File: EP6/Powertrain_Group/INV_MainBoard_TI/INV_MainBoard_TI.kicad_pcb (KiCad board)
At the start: 4 copper layers, 100 x 92 mm, 259 parts, among them IC1 LM26420Q0XMHX_NOPB, J1 FX26-30P-1SV, J10 CAN, J11 CAN, J12 CAN, J13 motorTemp, J14 LVBattery, J15 PWMDAC, J2 motorSense, J3 LVBattery, J4 JTAG, J5 current_DC, J6 to PhaseIsense, J7 phase control monitor, J8 current, J9 CAN, Q1 2N7002, Q2 2N7002, SW1 TS-1187A-B-A-B, U1 LM324D, U10 LM2903, U11 LM2903, U12 LM2903, U13 LM2903, U14 OPA340NA, U15 LM2903, U2 TPS5430DDAR, U21 OPA340NA, U22 tms320f28377s, U23 REF3133AQDBZRQ1, U24 REF3133AQDBZRQ1, U3 OPA340NA, U4 TCAN1042VDRQ1, U5 CAT24C256, U6 TCAN1042VDRQ1, U7 OPA340NA, U8 OPA340NA, U9 OPA340NA, Y1 ABM3BAIG-10.000MHZ-12-1Z-T

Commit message: update INV_MainBoard_TI to V1.1
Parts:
- removed JP2: TRST, Jumper:SolderJumper-2_P1.3mm_Bridged_Pad1.0x1.5mm
- removed U21: OPA340NA, Package_TO_SOT_SMD:SOT-23-5
- added C100: 680p, Capacitor_SMD:C_0402_1005Metric, F.Cu at (165.4, 125.6)
- added C101: 680p, Capacitor_SMD:C_0402_1005Metric, F.Cu at (154.1, 127.4)
- added C102: 680p, Capacitor_SMD:C_0402_1005Metric, F.Cu at (143.0, 129.7)
- added C103: 100n, Capacitor_SMD:C_0402_1005Metric, F.Cu at (179.7, 131.7)
- added C104: 100n, Capacitor_SMD:C_0402_1005Metric, F.Cu at (178.7, 127.3)
- added C105: 100n, Capacitor_SMD:C_0402_1005Metric, F.Cu at (118.6, 140.8)
- added C106: 100n, Capacitor_SMD:C_0402_1005Metric, F.Cu at (172.3, 114.5)
- added C107: 100n, Capacitor_SMD:C_0402_1005Metric, F.Cu at (167.7, 119.7)
- added C108: 100n, Capacitor_SMD:C_0402_1005Metric, F.Cu at (156.4, 121.5)
- added C109: 100n, Capacitor_SMD:C_0402_1005Metric, F.Cu at (145.3, 123.8)
- added C110: 100n, Capacitor_SMD:C_0402_1005Metric, F.Cu at (124.7, 115.6)
- added C111: 100n, Capacitor_SMD:C_0402_1005Metric, F.Cu at (128.1, 119.5)
- added C112: 22p, Capacitor_SMD:C_0402_1005Metric, F.Cu at (131.7, 58.1)
- added C113: 22p, Capacitor_SMD:C_0402_1005Metric, F.Cu at (131.7, 61.9)
- added C114: 22p, Capacitor_SMD:C_0402_1005Metric, F.Cu at (131.7, 68.8)
- added C115: 22p, Capacitor_SMD:C_0402_1005Metric, F.Cu at (131.7, 72.7)
- added C116: 4u7 10v, Capacitor_SMD:C_0402_1005Metric, F.Cu at (145.0, 61.6)
- added C117: 4u7 10v, Capacitor_SMD:C_0402_1005Metric, F.Cu at (145.0, 68.1)
- added C59: 43p, Capacitor_SMD:C_0402_1005Metric, F.Cu at (118.4, 113.3)
- added C85: 43p, Capacitor_SMD:C_0402_1005Metric, F.Cu at (120.0, 118.0)
- added C86: 100n, Capacitor_SMD:C_0402_1005Metric, F.Cu at (121.2, 115.6)
- added C95: 100n, Capacitor_SMD:C_0402_1005Metric, F.Cu at (127.5, 116.7)
- added C96: 1u, Capacitor_SMD:C_0402_1005Metric, F.Cu at (124.6, 143.1)
- added C99: 680p, Capacitor_SMD:C_0402_1005Metric, F.Cu at (178.2, 116.8)
- added D10: YELLOW LED, LED_SMD:LED_0603_1608Metric, F.Cu at (164.0, 106.8)
- added D11: LED50, LED_SMD:LED_0603_1608Metric, F.Cu at (165.6, 106.8)
- added D12: LED50, LED_SMD:LED_0603_1608Metric, F.Cu at (167.2, 106.8)
- added D13: LED50, LED_SMD:LED_0603_1608Metric, F.Cu at (168.8, 106.8)
- added D14: LED50, LED_SMD:LED_0603_1608Metric, F.Cu at (170.4, 106.8)
- added FB15: GZ1608D601TF, Capacitor_SMD:C_0603_1608Metric, F.Cu at (144.7, 121.3)
- added R78: 2k2, Resistor_SMD:R_0402_1005Metric, F.Cu at (165.7, 104.3)
- added SW2: BUT39, Button_Switch_SMD:SW_Tactile_SPST_NO_Straight_CK_PTS636Sx25SMTRLFS, F.Cu at (165.0, 113.7)
- added SW3: BUT58, Button_Switch_SMD:SW_Tactile_SPST_NO_Straight_CK_PTS636Sx25SMTRLFS, F.Cu at (169.6, 96.4)
- added U16: INA333AIDGK, PCM_Package_SO_AKL:MSOP-8_3x3mm_P0.65mm, F.Cu at (122.1, 113.3)
- added U17: INA333AIDGK, PCM_Package_SO_AKL:MSOP-8_3x3mm_P0.65mm, F.Cu at (123.8, 117.9)
- added U18: OPA340NA, Package_TO_SOT_SMD:SOT-23-5, F.Cu at (179.4, 129.5)
- C20, C21, C40, C41, C42, C43, C46, C47, C48, C49, C53, C54: value 0u1 -> 100n
- R17, R72: value 120R -> 90R
- R19, R20, R21, R22: value 10k -> 10k 0.1%
- R23, R24, R25, R26, R63, R64, R65: value 20k -> 10k
- R29, R55: value 22k -> 2k4
- R3: value 20k -> 1k
- R30, R54: value 82k -> 10k
- R31, R50, R52, R57, R59, R61: value 22k -> 10k
- R33, R51, R53, R56, R58, R60: value 82k -> 28k
- R34, R38: value 20k -> 10k 0.1%
- R35, R36, R37, R39, R40, R41, R43, R44, R45, R47, R48, R49: value 20k -> 100R
- R42, R46, R62: value 20k -> 2k2
- R68: value 10k -> 2k2
- SW1: footprint Button_Switch_SMD:SW_Push_1P1T_XKB_TS-1187A -> Button_Switch_SMD:SW_SPST_TL3342
- U1: value LM324D -> OPA340NA; footprint PCM_Package_SO_AKL:SOIC-14_3.9x8.7mm_P1.27mm -> Package_TO_SOT_SMD:SOT-23-5
- U14, U3, U7, U8, U9: value OPA340NA -> INA333AIDGK; footprint Package_TO_SOT_SMD:SOT-23-5 -> PCM_Package_SO_AKL:MSOP-8_3x3mm_P0.65mm
- moved U3 62.9 mm to (120.9, 143.1), turned to 180 degrees
- moved R34 60.5 mm to (119.1, 118.0), turned to 90 degrees
- moved R69 53.4 mm to (171.4, 78.5)
- moved R38 51.9 mm to (117.4, 113.3)
- moved C54 49.1 mm to (131.2, 125.8), turned to 180 degrees
- moved C53 48.9 mm to (131.1, 120.4)
- moved R26 48.4 mm to (178.7, 126.3), turned to 0 degrees
- moved R25 47.9 mm to (176.8, 129.5), turned to 90 degrees
- moved FB3 42.6 mm to (132.8, 119.4), turned to -90 degrees
- moved R62 42.6 mm to (168.7, 104.3), turned to -90 degrees
- moved FB5 38.5 mm to (119.9, 138.5)
- moved R46 38.0 mm to (167.7, 104.3), turned to -90 degrees
- moved FB6 36.9 mm to (178.4, 114.0)
- moved R42 30.3 mm to (166.7, 104.3), turned to -90 degrees
- moved R68 27.4 mm to (169.7, 104.3)
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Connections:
- net /Isense&motT_OCP&OTP/IsenseNode1/IN+ renamed /Isense&motT_OCP&OTP/U+
- net /Isense&motT_OCP&OTP/IsenseNode1/IN- renamed /Isense&motT_OCP&OTP/U-
- net /Isense&motT_OCP&OTP/IsenseNode2/IN+ renamed /Isense&motT_OCP&OTP/V+
- net /Isense&motT_OCP&OTP/IsenseNode2/IN- renamed /Isense&motT_OCP&OTP/V-
- net /Isense&motT_OCP&OTP/IsenseNode3/IN+ renamed /Isense&motT_OCP&OTP/W+
- net /Isense&motT_OCP&OTP/IsenseNode3/IN- renamed /Isense&motT_OCP&OTP/W-
- net /Isense&motT_OCP&OTP/OCPnode/filt5V renamed /Isense&motT_OCP&OTP/OCPnode/filt3V3
- net /Isense&motT_OCP&OTP/OCPnode1/filt5V renamed /Isense&motT_OCP&OTP/OCPnode1/filt3V3
- net /Isense&motT_OCP&OTP/OCPnode2/filt5V renamed /Isense&motT_OCP&OTP/OCPnode2/filt3V3
- net /Isense&motT_OCP&OTP/OCPnode3/filt5V renamed /Isense&motT_OCP&OTP/OCPnode3/filt3V3
- net /Isense&motT_OCP&OTP/filt5V renamed /Isense&motT_OCP&OTP/filt3V3
- net /MCU/TCK renamed /MCU/RTCK
- net Net-(J4-Pin_13) renamed /MCU/EMU0
- net Net-(J4-Pin_14) renamed /MCU/EMU1
- net Net-(J4-Pin_5) renamed /MCU/PD
- C21 pad 1: Net-(U3-V+) -> +5V
- C40 pad 1: Net-(U7-V+) -> +5V
- C41 pad 1: Net-(U8-V+) -> +5V
- C42 pad 1: Net-(U9-V+) -> +5V
- C43 pad 1: Net-(U14-V+) -> +5V
- C53 pad 1: Net-(U21-V+) -> Net-(U1-V+)
- C54 pad 1: Net-(U21--) -> Net-(U1--)
- FB1 pad 1: +5V -> +3V3
- FB10 pad 1: +3V3 -> Net-(U8-REF)
- FB10 pad 2: Net-(U21-V+) -> /Isense&motT_OCP&OTP/Vref_1.65V
- FB11 pad 1: +5V -> +3V3
- FB13 pad 1: +5V -> Net-(U9-REF)
- FB13 pad 2: Net-(U14-V+) -> /Isense&motT_OCP&OTP/Vref_1.65V
- FB3 pad 1: +5V -> +3V3
- FB3 pad 2: Net-(U3-V+) -> Net-(U1-V+)
- FB4 pad 1: +5V -> +3V3
- FB4 pad 2: Net-(U7-V+) -> Net-(U18-V+)
- FB5 pad 1: +5V -> Net-(U3-REF)
- FB5 pad 2: Net-(U8-V+) -> /Isense&motT_OCP&OTP/Vref_1.65V
- FB6 pad 1: +5V -> Net-(U7-REF)
- FB6 pad 2: Net-(U9-V+) -> /Isense&motT_OCP&OTP/Vref_1.65V
- FB7 pad 1: +5V -> +3V3
- FB8 pad 1: +5V -> +3V3
- FB9 pad 1: +5V -> +3V3
- J4 pad 2: Net-(J4-Pin_2) -> /MCU/TRST
- R19 pad 1: Net-(U1B--) -> /SIN+
- R19 pad 2: /EncoderDifVconverter/sin-3V3_out -> Net-(U16--)
- R20 pad 1: Net-(U1A--) -> /SIN-
- R20 pad 2: /EncoderDifVconverter/sin+3V3_out -> Net-(U16-+)
- R21 pad 1: Net-(U1D--) -> /COS+
- R21 pad 2: /EncoderDifVconverter/cos+3V3_out -> Net-(U17--)
- R22 pad 1: Net-(U1C--) -> /COS-
- R22 pad 2: /EncoderDifVconverter/cos-3V3_out -> Net-(U17-+)
- R23 pad 1: /EncoderDifVconverter/sin-3V3_out -> Net-(U1-V+)
- R23 pad 2: GND -> Net-(U1--)
- R24 pad 1: /EncoderDifVconverter/sin+3V3_out -> Net-(U1--)
- R25 pad 1: /EncoderDifVconverter/cos+3V3_out -> Net-(U18-V+)
- R25 pad 2: GND -> Net-(U18--)
- R26 pad 1: /EncoderDifVconverter/cos-3V3_out -> Net-(U18--)
- R34 pad 1: Net-(U3-+) -> Net-(U17-+)
- R34 pad 2: /Isense&motT_OCP&OTP/Vref_1.65V -> Net-(U17--)
- R35 pad 2: Net-(U3-+) -> Net-(U7--)
- R36 pad 2: Net-(U3--) -> Net-(U7-+)
- R37 pad 1: Net-(U3--) -> Net-(R37-Pad1)
- R37 pad 2: /Isense&motT_OCP&OTP/Isense_DC -> Net-(R37-Pad2)
- R38 pad 1: Net-(U7-+) -> Net-(U16-+)
- R38 pad 2: /Isense&motT_OCP&OTP/Vref_1.65V -> Net-(U16--)
- R39 pad 2: Net-(U7-+) -> Net-(U8--)
- R40 pad 2: Net-(U7--) -> Net-(U8-+)
- R41 pad 1: Net-(U7--) -> Net-(R41-Pad1)
- R41 pad 2: /Isense&motT_OCP&OTP/Isense_U -> Net-(R41-Pad2)
- R42 pad 1: Net-(U8-+) -> /MCU/LED50
- R42 pad 2: /Isense&motT_OCP&OTP/Vref_1.65V -> Net-(D11-A)
- R43 pad 2: Net-(U8-+) -> Net-(U9--)
- R44 pad 2: Net-(U8--) -> Net-(U9-+)
- R45 pad 1: Net-(U8--) -> Net-(R45-Pad1)
- R45 pad 2: /Isense&motT_OCP&OTP/Isense_V -> Net-(R45-Pad2)
- R46 pad 1: Net-(U9-+) -> /MCU/LED51
- R46 pad 2: /Isense&motT_OCP&OTP/Vref_1.65V -> Net-(D12-A)
- R47 pad 2: Net-(U9-+) -> Net-(U14--)
- R48 pad 2: Net-(U9--) -> Net-(U14-+)
- R49 pad 1: Net-(U9--) -> Net-(R49-Pad1)
- R49 pad 2: /Isense&motT_OCP&OTP/Isense_W -> Net-(R49-Pad2)
- R62 pad 1: Net-(U14-+) -> /MCU/LED52
- R62 pad 2: /Isense&motT_OCP&OTP/Vref_1.65V -> Net-(D13-A)
- R63 pad 2: Net-(U14-+) -> Net-(U3--)
- R64 pad 2: Net-(U14--) -> Net-(U3-+)
- R65 pad 1: Net-(U14--) -> Net-(R65-Pad1)
- R65 pad 2: /T_mot -> Net-(R65-Pad2)
- R68 pad 1: Net-(U21-V+) -> /MCU/LED53
- R68 pad 2: Net-(U21--) -> Net-(D14-A)
- R69 pad 1: Net-(U21--) -> +3V3
- R69 pad 2: GND -> /MCU/RST
- TP5 pad 1: /EncoderDifVconverter/sin-3V3_out -> /EncoderDifVconverter/sin+3V3_out
- TP6 pad 1: /EncoderDifVconverter/sin+3V3_out -> /EncoderDifVconverter/Vref_1.65V
- TP8 pad 1: /EncoderDifVconverter/cos-3V3_out -> /EncoderDifVconverter/Vref_1.65V
- U1 pad 1: Net-(U1A--) -> /EncoderDifVconverter/Vref_1.65V
- U1 pad 2: Net-(U1A--) -> GND
- U1 pad 3: /SIN- -> /EncoderDifVconverter/Vref_1.65V
- U1 pad 4: +5V -> Net-(U1--)
- U1 pad 5: /SIN+ -> Net-(U1-V+)
- U14 pad 1: /T_mot -> Net-(R49-Pad2)
- U14 pad 2: GND -> Net-(U14--)
- U14 pad 4: Net-(U14--) -> GND
- U14 pad 5: Net-(U14-V+) -> Net-(U14-REF)
- U22 pad 103: unconnected-(U22D-GPIO58-Pad103) -> /MCU/Button58
- U22 pad 47: /EncoderDifVconverter/sin-3V3_out -> /EncoderDifVconverter/Vref_1.65V
- U22 pad 49: /EncoderDifVconverter/cos-3V3_out -> /EncoderDifVconverter/Vref_1.65V
- U22 pad 86: unconnected-(U22C-GPIO39-Pad86) -> /MCU/Button39
- U22 pad 92: unconnected-(U22B-ERRORSTS-Pad92) -> Net-(U22B-ERRORSTS)
- U22 pad 94: unconnected-(U22D-GPIO50-Pad94) -> /MCU/LED50
- U22 pad 95: unconnected-(U22D-GPIO51-Pad95) -> /MCU/LED51
- U22 pad 96: unconnected-(U22D-GPIO52-Pad96) -> /MCU/LED52
- U22 pad 97: unconnected-(U22D-GPIO53-Pad97) -> /MCU/LED53
- U3 pad 1: /Isense&motT_OCP&OTP/Isense_DC -> Net-(R65-Pad2)
- U3 pad 2: GND -> Net-(U3--)
- U3 pad 4: Net-(U3--) -> GND
- U3 pad 5: Net-(U3-V+) -> Net-(U3-REF)
- U7 pad 1: /Isense&motT_OCP&OTP/Isense_U -> Net-(R37-Pad2)
- U7 pad 2: GND -> Net-(U7--)
- U7 pad 4: Net-(U7--) -> GND
- U7 pad 5: Net-(U7-V+) -> Net-(U7-REF)
- U8 pad 1: /Isense&motT_OCP&OTP/Isense_V -> Net-(R41-Pad2)
- U8 pad 2: GND -> Net-(U8--)
- U8 pad 4: Net-(U8--) -> GND
- U8 pad 5: Net-(U8-V+) -> Net-(U8-REF)
- U9 pad 1: /Isense&motT_OCP&OTP/Isense_W -> Net-(R45-Pad2)
- U9 pad 2: GND -> Net-(U9--)
- U9 pad 4: Net-(U9--) -> GND
- U9 pad 5: Net-(U9-V+) -> Net-(U9-REF)
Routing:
- net +3V3: track 220.0 -> 317.6 mm, vias 4 -> 12
- net /EncoderDifVconverter/Vref_1.65V: track 0.00 -> 56.1 mm
- net /Isense&motT_OCP&OTP/Vref_1.65V: track 60.8 -> 99.0 mm, vias 7 -> 6
- net /T_mot: track 98.0 -> 63.7 mm
- net GND: track 245.7 -> 273.2 mm, vias 168 -> 180
- net /MCU/TRST: track 30.1 -> 52.2 mm
- net +5V: track 76.6 -> 98.1 mm, vias 17 -> 13
- net Net-(J4-Pin_2): track 19.1 -> 0.00 mm
- net /EncoderDifVconverter/cos-3V3_out: track 16.8 -> 0.00 mm
- net Net-(U1B--): track 15.1 -> 0.00 mm
- net /EncoderDifVconverter/sin-3V3_out: track 12.9 -> 0.00 mm
- net /Isense&motT_OCP&OTP/Isense_V: track 42.2 -> 32.1 mm
- net Net-(U1A--): track 9.05 -> 0.00 mm
- net /MCU/LED53: track 0.00 -> 8.80 mm
- net /MCU/Button58: track 0.00 -> 8.49 mm
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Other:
- board text added: "+ DC Isense -"
- board text added: "50"
- board text added: "51"
- board text added: "52"
- board text added: "53"
- board text added: "5V G U+ U-"
- board text added: "5V G V+ V-"
- board text added: "5V G W+ W-"
- board text added: "BUT 39"
- board text added: "BUT 58"
- board text added: "C+"
- board text added: "C-"
- board text added: "EP6 INV_MainBoard_TI V1.1 25/02/22 Jack Kuo"
- board text added: "ERR"
- board text added: "GND GND"
- board text added: "OTP threshold"
- board text added: "Phase Isense"
- board text added: "S+"
- board text added: "S-"
- board text added: "mot Temp"
- board text added: "motor TEMP"
- board text removed: "DC Isense"
- board text removed: "EP6 INV_MainBoard_TI V1.0 25/02/19 Jack Kuo"
- board text removed: "WVU Isense"
- board text removed: "motor TEMP OTP threshold"

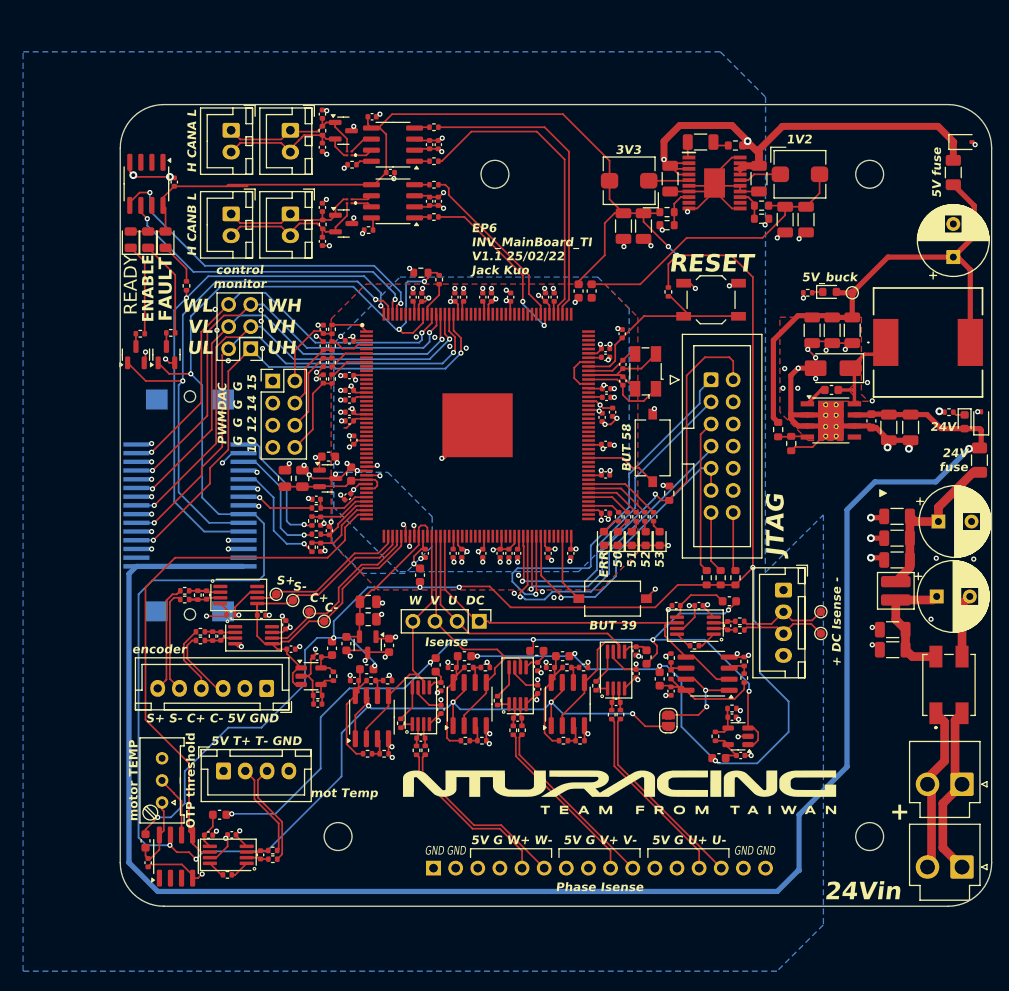
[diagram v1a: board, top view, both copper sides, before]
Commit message: update INV_MainBoard_TI to V1.2
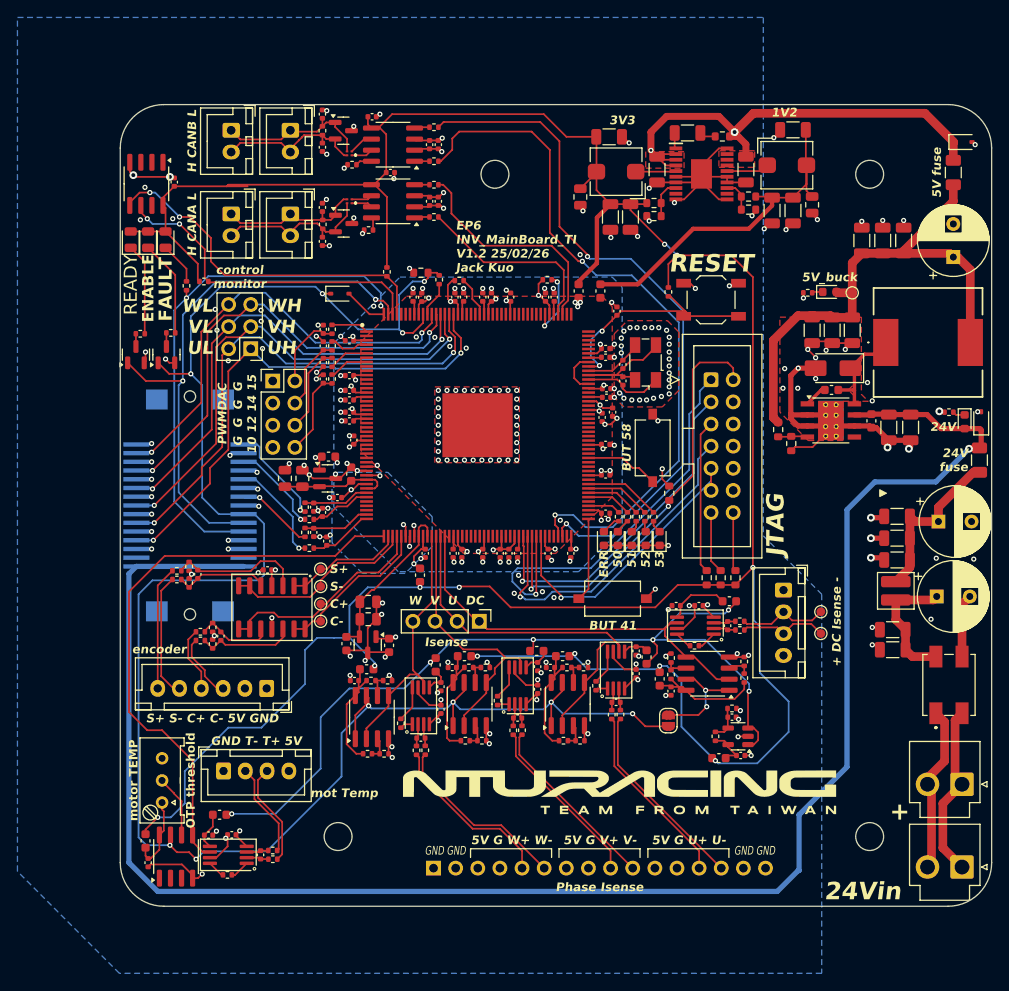
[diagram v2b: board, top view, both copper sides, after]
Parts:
- removed C111: 100n, Capacitor_SMD:C_0402_1005Metric
- removed FB3: GZ1608D601TF, Capacitor_SMD:C_0603_1608Metric
- removed R24: 10k, Resistor_SMD:R_0402_1005Metric
- removed U1: OPA340NA, Package_TO_SOT_SMD:SOT-23-5
- removed U17: INA333AIDGK, PCM_Package_SO_AKL:MSOP-8_3x3mm_P0.65mm
- added C118: 22u 25V, Capacitor_SMD:C_1206_3216Metric, F.Cu at (193.6, 72.6)
- added C119: 22u 25V, Capacitor_SMD:C_1206_3216Metric, F.Cu at (196.0, 72.6)
- added C120: 22u 25V, Capacitor_SMD:C_1206_3216Metric, F.Cu at (198.4, 72.6)
- added D15: B5818WS, Diode_SMD:D_SOD-323, F.Cu at (133.7, 78.7)
- added R79: 1k, Resistor_SMD:R_0402_1005Metric, F.Cu at (147.4, 77.2)
- added R80: 1k, Resistor_SMD:R_0402_1005Metric, F.Cu at (157.5, 77.1)
- added R81: 1k, Resistor_SMD:R_0402_1005Metric, F.Cu at (118.1, 77.3)
- added R82: 1k, Resistor_SMD:R_0402_1005Metric, F.Cu at (139.1, 76.2)
- added R83: 20k 0.1%, Resistor_SMD:R_0402_1005Metric, F.Cu at (116.4, 111.9)
- C110, C54: value 100n -> 1u; footprint Capacitor_SMD:C_0402_1005Metric -> Capacitor_SMD:C_0805_2012Metric
- C52, C57, C58: value 1u -> 100n
- C53, C95: value 100n -> 10u; footprint Capacitor_SMD:C_0402_1005Metric -> Capacitor_SMD:C_1206_3216Metric
- R11, R32, R5: value 1k -> 10k
- R23: value 10k -> 20k 0.1%
- R34, R38: value 10k 0.1% -> 20k 0.1%
- U16: value INA333AIDGK -> LM324D; footprint PCM_Package_SO_AKL:MSOP-8_3x3mm_P0.65mm -> PCM_Package_SO_AKL:SOIC-14_3.9x8.7mm_P1.27mm
- moved C53 81.5 mm to (185.7, 59.9)
- moved C54 80.6 mm to (187.9, 68.5), turned to -90 degrees
- moved C95 67.2 mm to (164.6, 60.7), turned to 0 degrees
- moved C110 60.4 mm to (161.3, 67.6), turned to -90 degrees
- moved R23 14.3 mm to (119.1, 118.9), turned to 90 degrees
- moved C86 6.67 mm to (125.4, 110.4)
- moved TP5 5.87 mm to (131.5, 110.3)
- moved U16 4.06 mm to (125.9, 114.7), turned to -90 degrees
- moved C97 3.81 mm to (130.7, 106.1), turned to -90 degrees
- moved TP6 3.58 mm to (131.5, 112.3)
- moved R38 3.45 mm to (116.4, 110.0)
- moved R76 3.09 mm to (129.7, 106.1), turned to 90 degrees
- moved C32 2.67 mm to (165.5, 80.7)
- moved C59 2.58 mm to (117.4, 110.9)
- moved R19 2.47 mm to (115.0, 110.5)
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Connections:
- C110 pad 1: /EncoderDifVconverter/Vref_1.65V -> +3V3
- C112 pad 1: /Peripherals/CANAL -> /Peripherals/CANBL
- C113 pad 1: /Peripherals/CANAH -> /Peripherals/CANBH
- C114 pad 1: /Peripherals/CANBL -> /Peripherals/CANAL
- C115 pad 1: /Peripherals/CANBH -> /Peripherals/CANAH
- C53 pad 1: Net-(U1-V+) -> +1V2
- C54 pad 1: Net-(U1--) -> +1V2
- C59 pad 1: Net-(U16--) -> Net-(U16A-+)
- C59 pad 2: Net-(U16-+) -> Net-(U16B-+)
- C85 pad 1: Net-(U17--) -> Net-(U16C-+)
- C85 pad 2: Net-(U17-+) -> Net-(U16D-+)
- C95 pad 1: +5V -> +3V3
- D17 pad 1: /Peripherals/CANBL -> /Peripherals/CANAL
- D17 pad 2: /Peripherals/CANBH -> /Peripherals/CANAH
- D8 pad 1: /Peripherals/CANAL -> /Peripherals/CANBL
- D8 pad 2: /Peripherals/CANAH -> /Peripherals/CANBH
- FL2 pad 3: /Peripherals/CANAL -> /Peripherals/CANBL
- FL2 pad 4: /Peripherals/CANAH -> /Peripherals/CANBH
- FL3 pad 3: /Peripherals/CANBL -> /Peripherals/CANAL
- FL3 pad 4: /Peripherals/CANBH -> /Peripherals/CANAH
- J10 pad 1: /Peripherals/CANAL -> /Peripherals/CANBL
- J10 pad 2: /Peripherals/CANAH -> /Peripherals/CANBH
- J11 pad 1: /Peripherals/CANBL -> /Peripherals/CANAL
- J11 pad 2: /Peripherals/CANBH -> /Peripherals/CANAH
- J12 pad 1: /Peripherals/CANBL -> /Peripherals/CANAL
- J12 pad 2: /Peripherals/CANBH -> /Peripherals/CANAH
- J9 pad 1: /Peripherals/CANAL -> /Peripherals/CANBL
- J9 pad 2: /Peripherals/CANAH -> /Peripherals/CANBH
- R15 pad 1: /MCU/CANA_TX -> /MCU/CANB_TX
- R16 pad 1: /MCU/CANA_RX -> /MCU/CANB_RX
- R17 pad 1: /Peripherals/CANAH -> /Peripherals/CANBH
- R17 pad 2: /Peripherals/CANAL -> /Peripherals/CANBL
- R19 pad 2: Net-(U16--) -> Net-(U16A-+)
- R20 pad 2: Net-(U16-+) -> Net-(U16B-+)
- R21 pad 2: Net-(U17--) -> Net-(U16C-+)
- R22 pad 2: Net-(U17-+) -> Net-(U16D-+)
- R23 pad 1: Net-(U1-V+) -> Net-(U16D-+)
- R23 pad 2: Net-(U1--) -> GND
- R34 pad 1: Net-(U17-+) -> GND
- R34 pad 2: Net-(U17--) -> Net-(U16C-+)
- R38 pad 1: Net-(U16-+) -> GND
- R38 pad 2: Net-(U16--) -> Net-(U16A-+)
- R70 pad 1: /MCU/CANB_TX -> /MCU/CANA_TX
- R71 pad 1: /MCU/CANB_RX -> /MCU/CANA_RX
- R72 pad 1: /Peripherals/CANBH -> /Peripherals/CANAH
- R72 pad 2: /Peripherals/CANBL -> /Peripherals/CANAL
- SW2 pad 2: /MCU/Button39 -> /MCU/Button41
- TP6 pad 1: /EncoderDifVconverter/Vref_1.65V -> /EncoderDifVconverter/sin-3V3_out
- TP8 pad 1: /EncoderDifVconverter/Vref_1.65V -> /EncoderDifVconverter/cos-3V3_out
- U16 pad 1: unconnected-(U16-RG-Pad1) -> /EncoderDifVconverter/sin+3V3_out
- U16 pad 2: Net-(U16--) -> /EncoderDifVconverter/sin+3V3_out
- U16 pad 3: Net-(U16-+) -> Net-(U16A-+)
- U16 pad 4: GND -> +5V
- U16 pad 5: /EncoderDifVconverter/Vref_1.65V -> Net-(U16B-+)
- U16 pad 6: /EncoderDifVconverter/sin+3V3_out -> /EncoderDifVconverter/sin-3V3_out
- U16 pad 7: +5V -> /EncoderDifVconverter/sin-3V3_out
- U16 pad 8: unconnected-(U16-RG-Pad8) -> /EncoderDifVconverter/cos+3V3_out
- U22 pad 139: /MCU/CANB_TX -> /MCU/BOOT1
- U22 pad 140: /MCU/CANB_RX -> unconnected-(U22D-GPIO73-Pad140)
- U22 pad 154: unconnected-(U22D-GPIO84-Pad154) -> /MCU/BOOT0
- U22 pad 38: unconnected-(U22E-ADCINA5-Pad38) -> /T_filt_U
- U22 pad 39: /Vsense_filt_DC -> /T_filt_V
- U22 pad 40: /T_filt_U -> unconnected-(U22E-ADCINA3-Pad40)
- U22 pad 41: /T_filt_V -> unconnected-(U22E-ADCINA2-Pad41)
- U22 pad 42: /T_filt_W -> unconnected-(U22E-ADCINA1-Pad42)
- U22 pad 43: /T_mot -> /Vsense_filt_DC
- U22 pad 44: unconnected-(U22E-ADCIN14-Pad44) -> /T_filt_W
- U22 pad 45: unconnected-(U22E-ADCIN15-Pad45) -> /T_mot
- U22 pad 47: /EncoderDifVconverter/Vref_1.65V -> /EncoderDifVconverter/sin-3V3_out
- U22 pad 49: /EncoderDifVconverter/Vref_1.65V -> /EncoderDifVconverter/cos-3V3_out
- U22 pad 85: unconnected-(U22C-GPIO38-Pad85) -> /MCU/CANB_TX
- U22 pad 86: /MCU/Button39 -> /MCU/CANB_RX
- U22 pad 89: unconnected-(U22C-GPIO41-Pad89) -> /MCU/Button41
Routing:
- net /MCU/CANB_TX: track 20.6 -> 80.8 mm
- net /MCU/CANB_RX: track 20.2 -> 79.9 mm, vias 0 -> 2
- net /EncoderDifVconverter/Vref_1.65V: track 56.1 -> 0.00 mm
- net /EncoderDifVconverter/sin-3V3_out: track 0.00 -> 22.3 mm
- net +3V3: track 317.6 -> 337.5 mm, vias 12 -> 11
- net /EncoderDifVconverter/cos-3V3_out: track 0.00 -> 18.4 mm
- net Net-(U16A-+): track 0.00 -> 15.4 mm
- net /MCU/CANA_TX: track 35.3 -> 22.2 mm
- net Net-(U16D-+): track 0.00 -> 11.3 mm
- net Net-(U16B-+): track 0.00 -> 10.9 mm
- net /MCU/Button41: track 0.00 -> 9.61 mm
- net /MCU/CANA_RX: track 35.1 -> 26.2 mm
- net Net-(U16C-+): track 0.00 -> 8.88 mm
- net /MCU/Button39: track 7.94 -> 0.00 mm
- net /MCU/BOOT1: track 0.00 -> 7.88 mm, vias 0 -> 2
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- added copper zone on F.Cu, net +5V
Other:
- board text added: "BUT 41"
- board text added: "EP6 INV_MainBoard_TI V1.2 25/02/26 Jack Kuo"
- board text added: "GND T- T+ 5V"
- board text removed: "5V T+ T- GND"
- board text removed: "BUT 39"
- board text removed: "EP6 INV_MainBoard_TI V1.1 25/02/22 Jack Kuo"

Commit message: update INV_MainBoard_TI to V1.3
fix negative feedback mistake in 1.65 Vref
and some other minor fix
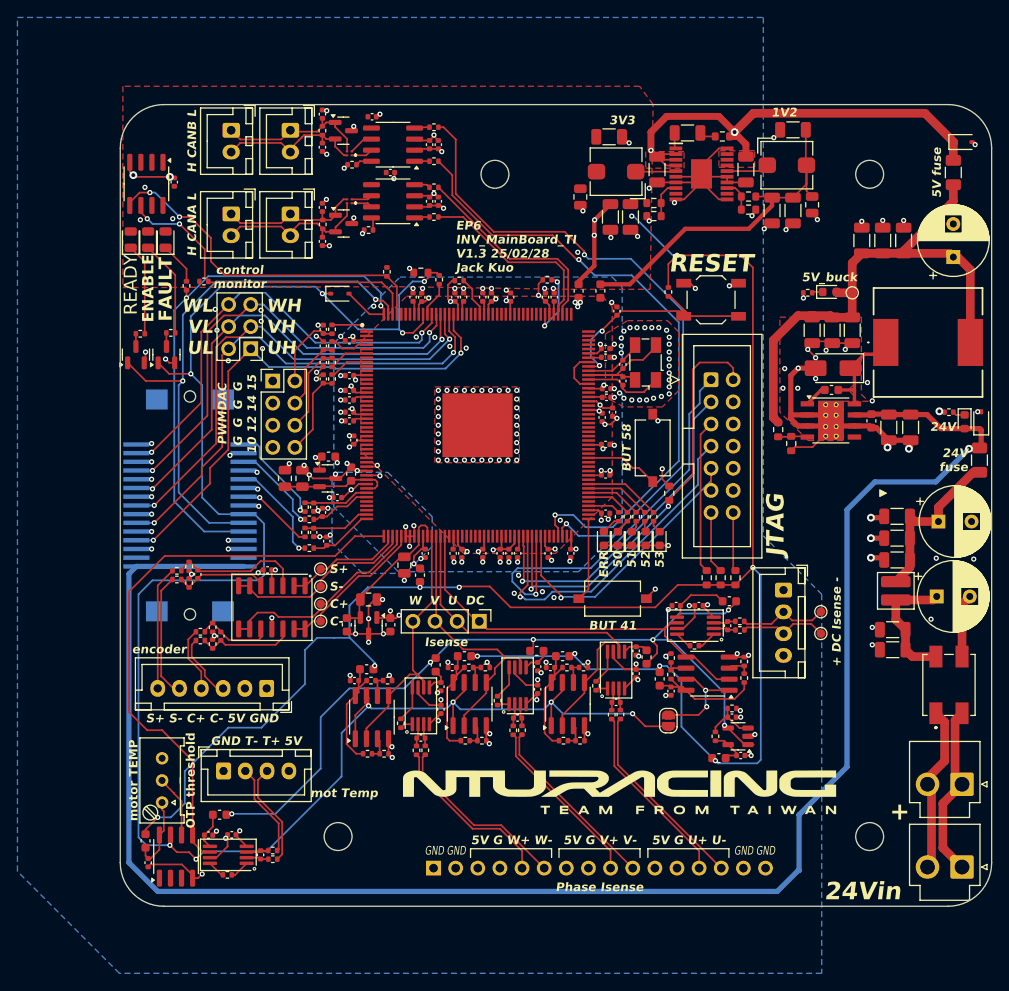
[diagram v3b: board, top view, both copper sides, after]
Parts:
- R25, R26: value 10k -> 10k 0.1%
- R37: value 100R -> 10M
- R41, R45, R49: value 100R -> 100k
- R65: value 10k -> 10M
- moved C89 5.91 mm to (141.1, 109.8), turned to -90 degrees
- moved C93 2.37 mm to (139.5, 116.7)
- moved C90 2.26 mm to (137.0, 113.8)
- moved U24 2.20 mm to (137.0, 116.8)
- moved C94 2.16 mm to (134.5, 116.7)
- moved R71 0.30 mm to (144.5, 66.5)
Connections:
- net /Isense&motT_OCP&OTP/IsenseNode4/IN+ renamed /Isense&motT_OCP&OTP/Motor_temp/IN+
- net /Isense&motT_OCP&OTP/IsenseNode4/IN- renamed /Isense&motT_OCP&OTP/Motor_temp/IN-
- net /Isense&motT_OCP&OTP/filt3V3 renamed Net-(U15C-V+)
- net /MCU/PWMDAC_13 renamed /MCU/PWMDAC_14
- C104 pad 1: Net-(U18--) -> Net-(U18-+)
- R25 pad 2: Net-(U18--) -> Net-(U18-+)
- R26 pad 1: Net-(U18--) -> Net-(U18-+)
- U18 pad 3: /Isense&motT_OCP&OTP/Vref_1.65V -> Net-(U18-+)
- U18 pad 4: Net-(U18--) -> /Isense&motT_OCP&OTP/Vref_1.65V
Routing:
- net +3V3: track 337.5 -> 229.4 mm, vias 11 -> 13
- net /MCU/CANB_TX: track 80.8 -> 73.0 mm
- net Net-(U18-+): track 0.00 -> 6.29 mm
- net Net-(U18--): track 3.92 -> 0.00 mm
- net /Isense&motT_OCP&OTP/Vref_1.65V: track 99.0 -> 95.8 mm
- net /MCU/CANB_RX: track 79.9 -> 77.4 mm
- net /MCU/CANA_RX: track 26.2 -> 24.2 mm
- net /MCU/VDDA_BD: track 19.2 -> 17.4 mm
- net GND: track 273.3 -> 271.7 mm, vias 251 -> 252
- net /EncoderDifVconverter/cos-3V3_out: track 18.4 -> 17.8 mm
- net /EncoderDifVconverter/cos+3V3_out: track 25.1 -> 24.5 mm
- net +5V: track 91.9 -> 92.5 mm, vias 12 -> 13
- added copper zone on F.Cu, net +3V3
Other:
- board text added: "EP6 INV_MainBoard_TI V1.3 25/02/28 Jack Kuo"
- board text removed: "EP6 INV_MainBoard_TI V1.2 25/02/26 Jack Kuo"
